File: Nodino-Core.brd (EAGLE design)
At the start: 27.9 x 25.4 mm, 15 parts, among them CON1 NODINO-JTAGMODULE, CON2 USB-OTG_SHIELD, IC1 STM32F373CCT6, IC2 AP733333SAG, Q1 16MHz, Q2 32.768kHz

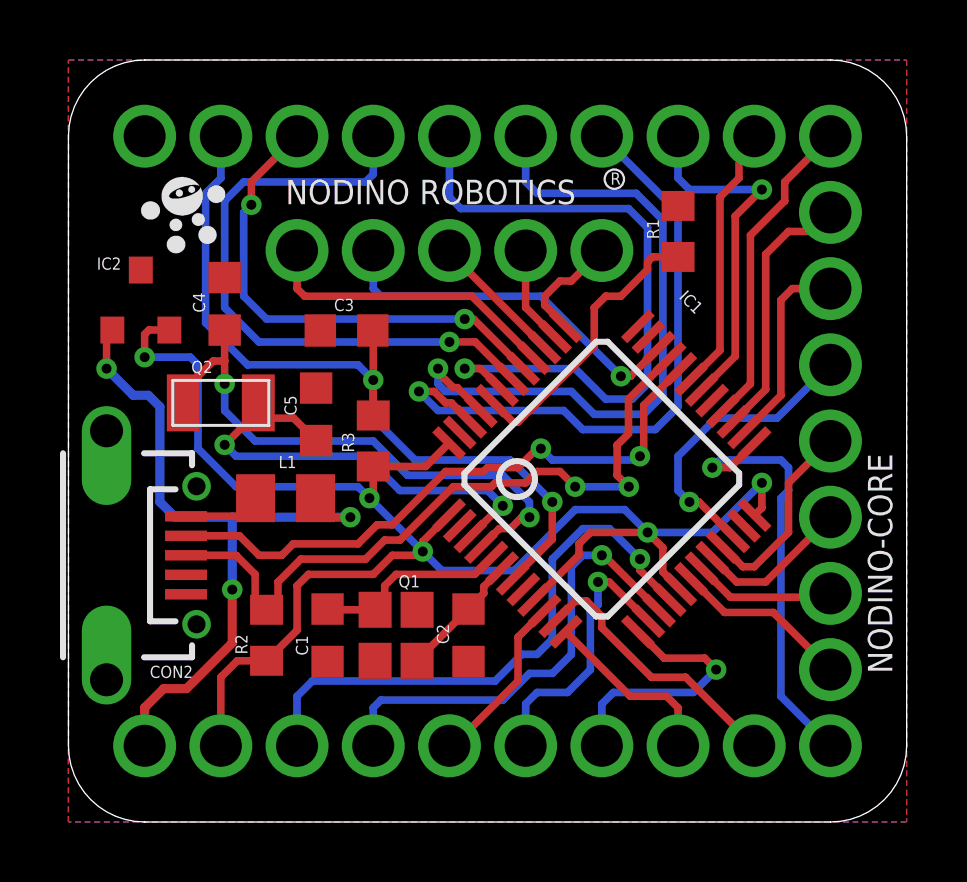
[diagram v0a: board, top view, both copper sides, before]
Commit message: added filter capacitors
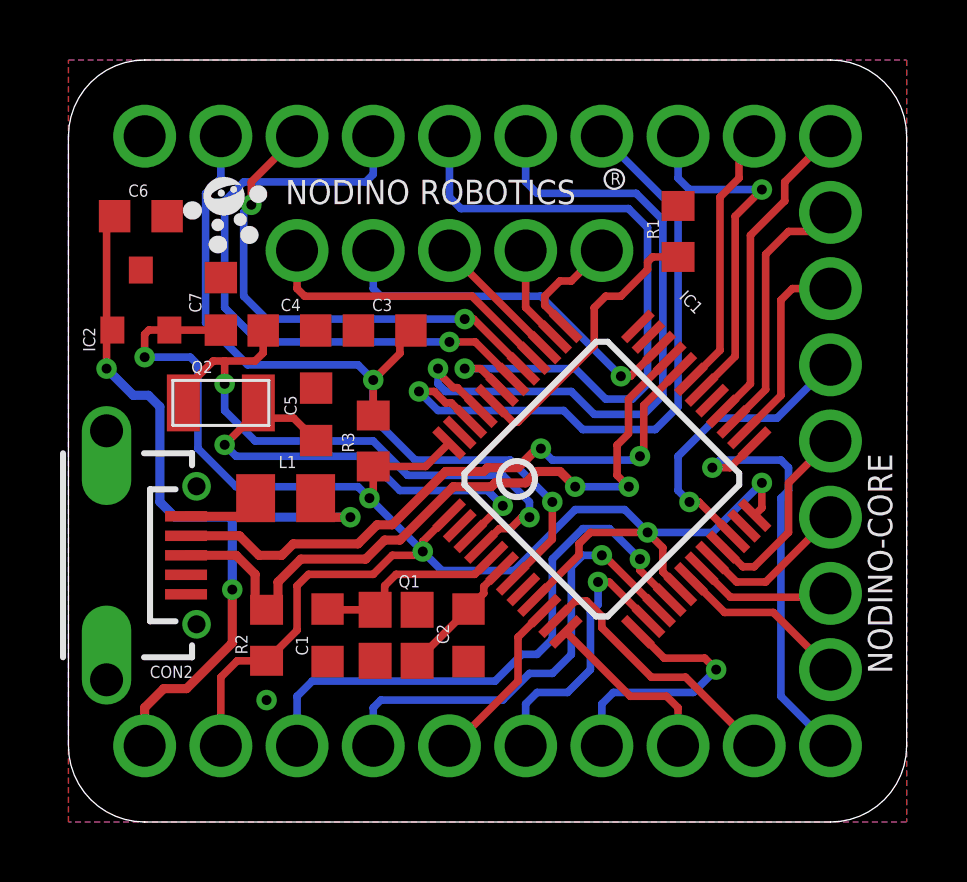
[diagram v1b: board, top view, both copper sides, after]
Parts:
- added C6, C7: 10uF, resistor:C0603K
- moved C4 2.33 mm to (7.37, 16.4), turned to 0 degrees
- moved C3 1.27 mm to (10.5, 16.4)
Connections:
- net +3V3: now also C7.1
- net +5V: now also C6.1
- net GND: now also C6.2, C7.2
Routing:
- net +5V: track 24.1 -> 28.1 mm
- net +3V3: track 54.4 -> 56.1 mm
- net 32K1: track 18.8 -> 19.9 mm
- net NRST: track 27.2 -> 27.7 mm
